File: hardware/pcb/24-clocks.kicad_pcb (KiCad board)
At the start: 2 copper layers, 89.9 x 42.4 mm, 2 parts, among them J1 Conn_01x03, J2 Conn_01x03

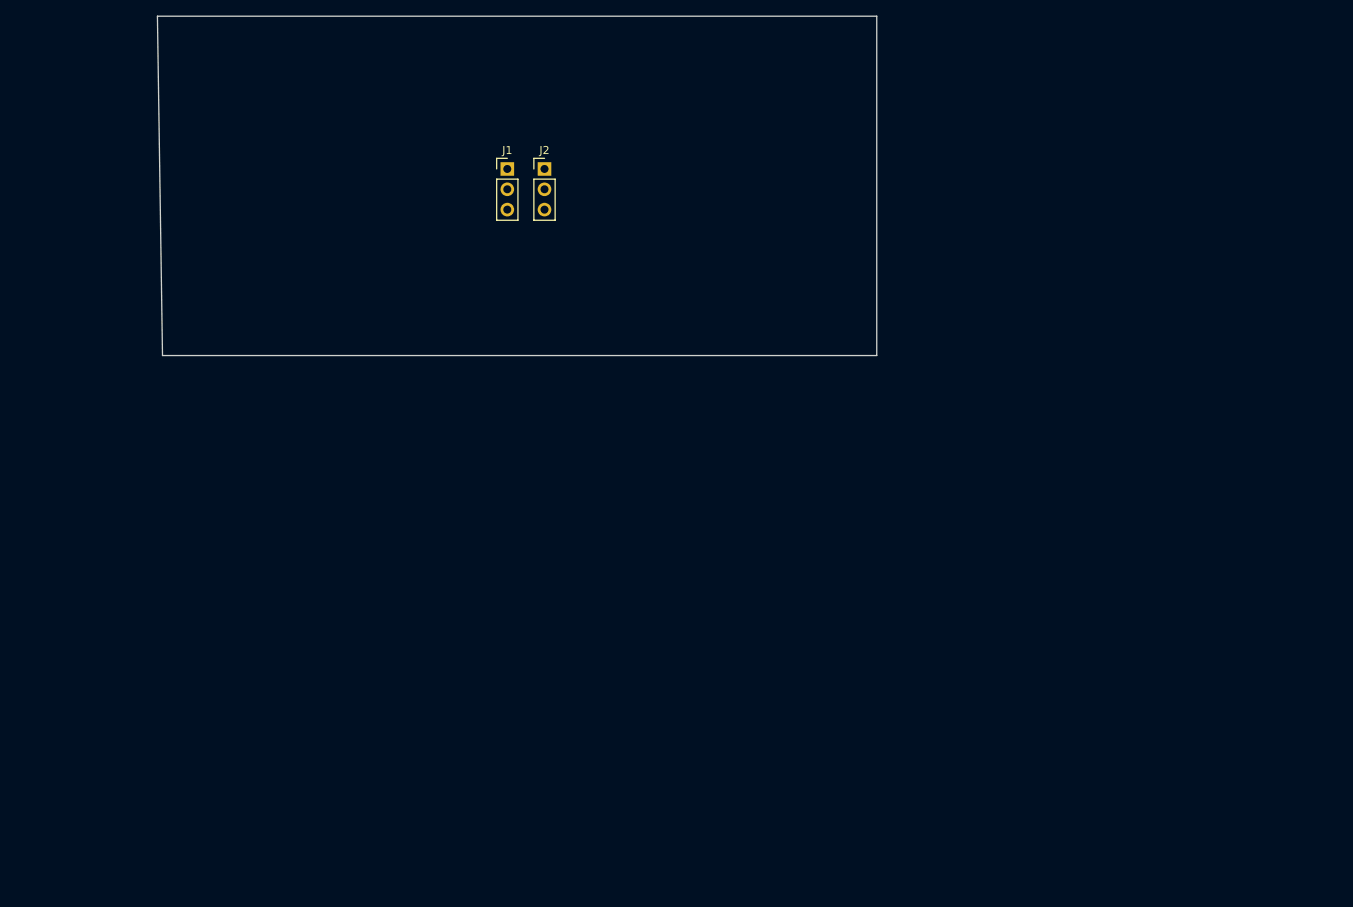
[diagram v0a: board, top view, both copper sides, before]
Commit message: Created footprints and archived project
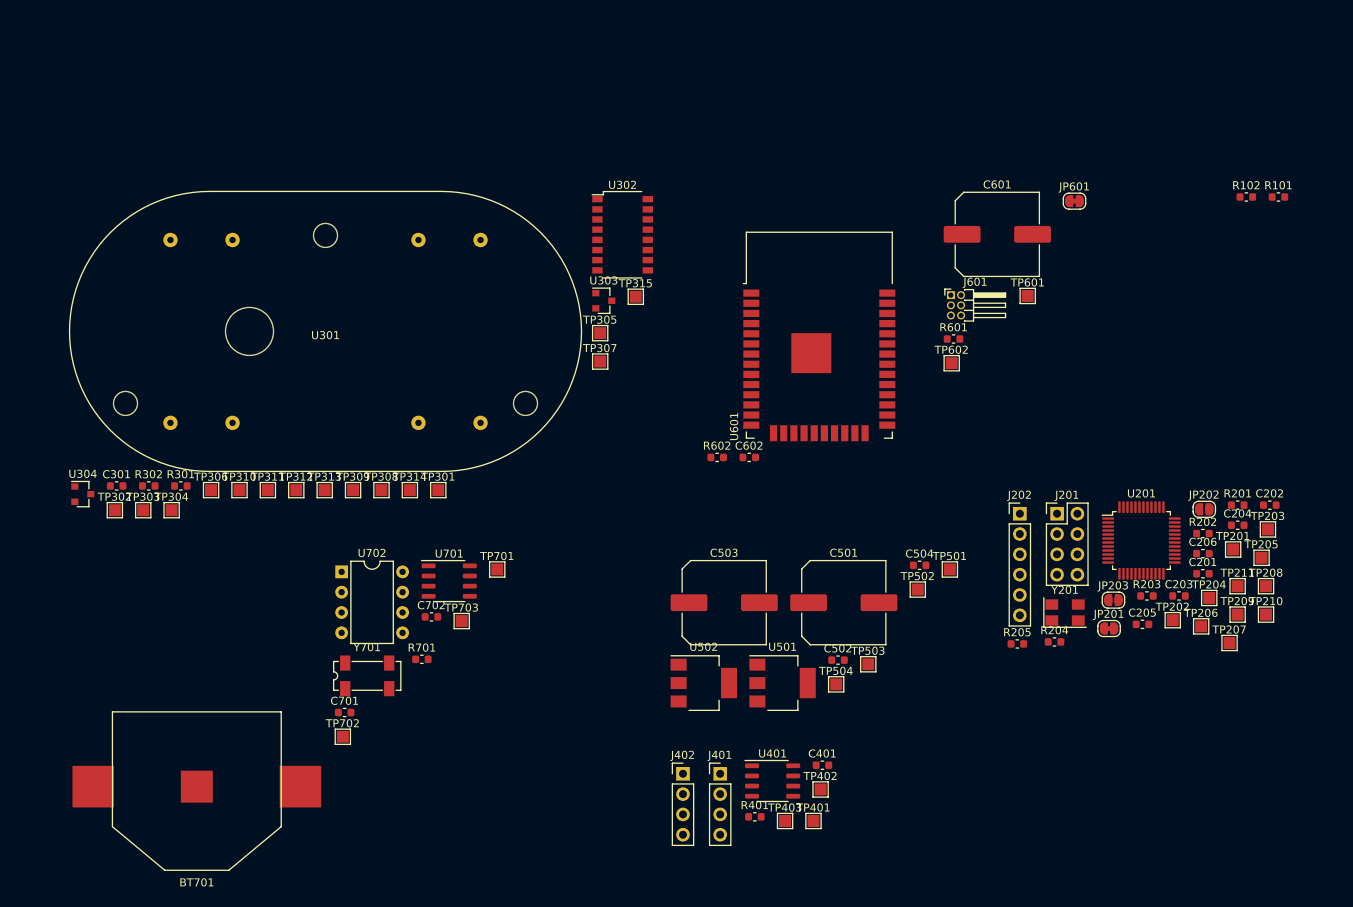
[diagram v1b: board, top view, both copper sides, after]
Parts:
- removed J1, J2: Conn_01x03, Connector_PinHeader_2.54mm:PinHeader_1x03_P2.54mm_Vertical
- added BT701: CR2032, mvl-footprints:BATT_WE_79523141, F.Cu at (106.4, 130.7)
- added C201: 100nF, Capacitor_SMD:C_0603_1608Metric, F.Cu at (232.2, 104.1)
- added C202: 100nF, Capacitor_SMD:C_0603_1608Metric, F.Cu at (240.5, 95.5)
- added C203: 100nF, Capacitor_SMD:C_0603_1608Metric, F.Cu at (229.2, 106.9)
- added C204: 100nF, Capacitor_SMD:C_0603_1608Metric, F.Cu at (236.5, 98.0)
- added C205: 20pF, Capacitor_SMD:C_0603_1608Metric, F.Cu at (224.6, 110.4)
- added C206: 20pF, Capacitor_SMD:C_0603_1608Metric, F.Cu at (232.2, 101.6)
- added C301: 100nF, Capacitor_SMD:C_0603_1608Metric, F.Cu at (96.4, 93.1)
- added C401: 100nF, Capacitor_SMD:C_0603_1608Metric, F.Cu at (184.6, 128.0)
- added C501: 22uF, Capacitor_SMD:C_Elec_10x10.2, F.Cu at (187.3, 107.7)
- added C502: 100nF, Capacitor_SMD:C_0603_1608Metric, F.Cu at (186.5, 114.9)
- added C503: 22uF, Capacitor_SMD:C_Elec_10x10.2, F.Cu at (172.3, 107.7)
- added C504: 100nF, Capacitor_SMD:C_0603_1608Metric, F.Cu at (196.7, 103.1)
- added C601: 22uF, Capacitor_SMD:C_Elec_10x10.2, F.Cu at (206.5, 61.7)
- added C602: 100nF, Capacitor_SMD:C_0603_1608Metric, F.Cu at (175.4, 89.6)
- added C701: 100nF, Capacitor_SMD:C_0603_1608Metric, F.Cu at (124.9, 121.5)
- added C702: 100nF, Capacitor_SMD:C_0603_1608Metric, F.Cu at (135.7, 109.5)
- added J201: ST-LINK, Connector_PinHeader_2.54mm:PinHeader_2x04_P2.54mm_Vertical, F.Cu at (213.9, 96.6)
- added J202: Debug UART, Connector_PinHeader_2.54mm:PinHeader_1x06_P2.54mm_Vertical, F.Cu at (209.3, 96.6)
- added J401: Conn_01x04, Connector_PinHeader_2.54mm:PinHeader_1x04_P2.54mm_Vertical, F.Cu at (171.8, 129.1)
- added J402: Conn_01x04, Connector_PinHeader_2.54mm:PinHeader_1x04_P2.54mm_Vertical, F.Cu at (167.2, 129.1)
- added J601: Conn_02x03_Odd_Even, Connector_PinHeader_1.27mm:PinHeader_2x03_P1.27mm_Horizontal, F.Cu at (200.7, 69.3)
- added JP201: Jumper_NC_Small, Jumper:SolderJumper-2_P1.3mm_Bridged_RoundedPad1.0x1.5mm, F.Cu at (220.4, 111.0)
- added JP202: Jumper_NO_Small, Jumper:SolderJumper-2_P1.3mm_Open_RoundedPad1.0x1.5mm, F.Cu at (232.3, 96.1)
- added JP203: Jumper_NO_Small, Jumper:SolderJumper-2_P1.3mm_Open_RoundedPad1.0x1.5mm, F.Cu at (221.0, 107.4)
- added JP601: Jumper_NC_Small, Jumper:SolderJumper-2_P1.3mm_Bridged_RoundedPad1.0x1.5mm, F.Cu at (216.1, 57.5)
- added R101: 5k, Resistor_SMD:R_0603_1608Metric, F.Cu at (241.6, 57.0)
- added R102: 5k, Resistor_SMD:R_0603_1608Metric, F.Cu at (237.6, 57.0)
- added R201: 4k7, Resistor_SMD:R_0603_1608Metric, F.Cu at (236.5, 95.5)
- added R202: 10k, Resistor_SMD:R_0603_1608Metric, F.Cu at (232.2, 99.1)
- added R203: 10k, Resistor_SMD:R_0603_1608Metric, F.Cu at (225.2, 106.9)
- added R204: 10k, Resistor_SMD:R_0603_1608Metric, F.Cu at (213.6, 112.6)
- added R205: 10k, Resistor_SMD:R_0603_1608Metric, F.Cu at (209.0, 112.9)
- added R301: 10k, Resistor_SMD:R_0603_1608Metric, F.Cu at (104.4, 93.1)
- added R302: 10k, Resistor_SMD:R_0603_1608Metric, F.Cu at (100.4, 93.1)
- added R401: 120E, Resistor_SMD:R_0603_1608Metric, F.Cu at (176.1, 134.5)
- added R601: 10k, Resistor_SMD:R_0603_1608Metric, F.Cu at (201.0, 74.8)
- added R602: 10k, Resistor_SMD:R_0603_1608Metric, F.Cu at (171.4, 89.6)
- added R701: 10k, Resistor_SMD:R_0603_1608Metric, F.Cu at (134.5, 114.8)
- added TP201: SWO, TestPoint:TestPoint_Pad_1.5x1.5mm, F.Cu at (235.9, 101.1)
- added TP202: uC-Rst, TestPoint:TestPoint_Pad_1.5x1.5mm, F.Cu at (228.4, 109.9)
- added TP203: SWDCLK, TestPoint:TestPoint_Pad_1.5x1.5mm, F.Cu at (240.3, 98.6)
- added TP204: SWDIO, TestPoint:TestPoint_Pad_1.5x1.5mm, F.Cu at (232.9, 107.1)
- added TP205: 3V3, TestPoint:TestPoint_Pad_1.5x1.5mm, F.Cu at (239.5, 102.1)
- added TP206: GND, TestPoint:TestPoint_Pad_1.5x1.5mm, F.Cu at (231.9, 110.7)
- added TP207: BOOT0, TestPoint:TestPoint_Pad_1.5x1.5mm, F.Cu at (235.5, 112.8)
- added TP208: BOOT1, TestPoint:TestPoint_Pad_1.5x1.5mm, F.Cu at (240.0, 105.7)
- added TP209: uC-Debug-Rx, TestPoint:TestPoint_Pad_1.5x1.5mm, F.Cu at (236.5, 109.2)
- added TP210: uC-Debug-Tx, TestPoint:TestPoint_Pad_1.5x1.5mm, F.Cu at (240.0, 109.2)
- added TP211: HW-Version, TestPoint:TestPoint_Pad_1.5x1.5mm, F.Cu at (236.5, 105.7)
- added TP301: MA1, TestPoint:TestPoint_Pad_1.5x1.5mm, F.Cu at (136.6, 93.7)
- added TP302: MA2, TestPoint:TestPoint_Pad_1.5x1.5mm, F.Cu at (96.1, 96.2)
- added TP303: M-Rst, TestPoint:TestPoint_Pad_1.5x1.5mm, F.Cu at (99.7, 96.2)
- added TP304: MA3, TestPoint:TestPoint_Pad_1.5x1.5mm, F.Cu at (103.2, 96.2)
- added TP305: M-A-CW, TestPoint:TestPoint_Pad_1.5x1.5mm, F.Cu at (156.8, 74.0)
- added TP306: M-A-Step, TestPoint:TestPoint_Pad_1.5x1.5mm, F.Cu at (108.2, 93.7)
- added TP307: MA4, TestPoint:TestPoint_Pad_1.5x1.5mm, F.Cu at (156.8, 77.6)
- added TP308: M-B-CW, TestPoint:TestPoint_Pad_1.5x1.5mm, F.Cu at (129.5, 93.7)
- added TP309: M-B-Step, TestPoint:TestPoint_Pad_1.5x1.5mm, F.Cu at (125.9, 93.7)
- added TP310: MB1, TestPoint:TestPoint_Pad_1.5x1.5mm, F.Cu at (111.7, 93.7)
- added TP311: MB2, TestPoint:TestPoint_Pad_1.5x1.5mm, F.Cu at (115.3, 93.7)
- added TP312: MB3, TestPoint:TestPoint_Pad_1.5x1.5mm, F.Cu at (118.8, 93.7)
- added TP313: MB4, TestPoint:TestPoint_Pad_1.5x1.5mm, F.Cu at (122.4, 93.7)
- added TP314: HAL-A, TestPoint:TestPoint_Pad_1.5x1.5mm, F.Cu at (133.0, 93.7)
- added TP315: HAL-B, TestPoint:TestPoint_Pad_1.5x1.5mm, F.Cu at (161.3, 69.5)
- added TP401: uC-RS485-Rx, TestPoint:TestPoint_Pad_1.5x1.5mm, F.Cu at (183.5, 135.0)
- added TP402: uC-RS485-DE, TestPoint:TestPoint_Pad_1.5x1.5mm, F.Cu at (184.4, 131.1)
- added TP403: uC-RS485-Tx, TestPoint:TestPoint_Pad_1.5x1.5mm, F.Cu at (179.9, 135.0)
- added TP501: +9V, TestPoint:TestPoint_Pad_1.5x1.5mm, F.Cu at (200.5, 103.6)
- added TP502: +5V, TestPoint:TestPoint_Pad_1.5x1.5mm, F.Cu at (196.5, 106.1)
- added TP503: +3V3, TestPoint:TestPoint_Pad_1.5x1.5mm, F.Cu at (190.3, 115.4)
- added TP504: GND, TestPoint:TestPoint_Pad_1.5x1.5mm, F.Cu at (186.3, 117.9)
- added TP601: uC-WiFi-Tx, TestPoint:TestPoint_Pad_1.5x1.5mm, F.Cu at (210.3, 69.4)
- added TP602: uC-WiFi-Rx, TestPoint:TestPoint_Pad_1.5x1.5mm, F.Cu at (200.8, 77.8)
- added TP701: I2C-SDA, TestPoint:TestPoint_Pad_1.5x1.5mm, F.Cu at (143.9, 103.6)
- added TP702: I2C-SCL, TestPoint:TestPoint_Pad_1.5x1.5mm, F.Cu at (124.6, 124.5)
- added TP703: RC2032, TestPoint:TestPoint_Pad_1.5x1.5mm, F.Cu at (139.5, 110.0)
- added U201: STM32F103C8Tx, Package_QFP:LQFP-48_7x7mm_P0.5mm, F.Cu at (224.5, 100.0)
- added U301: VID28-05, mvl-footprints:vid_28_05, F.Cu at (122.5, 73.8)
- added U302: VID66-08, Package_SO:SOP-16_4.4x10.4mm_P1.27mm, F.Cu at (159.6, 61.7)
- added U303: AH3572, Package_TO_SOT_SMD:SOT-23, F.Cu at (157.3, 70.0)
- added U304: AH3572, Package_TO_SOT_SMD:SOT-23, F.Cu at (92.1, 94.2)
- added U401: MAX3485, Package_SO:SO-8_3.9x4.9mm_P1.27mm, F.Cu at (178.4, 130.0)
- added U501: AMS1117-5.0, Package_TO_SOT_SMD:SOT-223-3_TabPin2, F.Cu at (179.6, 117.8)
- added U502: AMS1117-3.3, Package_TO_SOT_SMD:SOT-223-3_TabPin2, F.Cu at (169.8, 117.8)
- added U601: ESP32-WROOM-32D, RF_Module:ESP32-WROOM-32, F.Cu at (184.2, 77.3)
- added U701: 24LC512, Package_SO:SO-8_3.9x4.9mm_P1.27mm, F.Cu at (137.9, 105.0)
- added U702: DS1307+, Package_DIP:DIP-8_W7.62mm, F.Cu at (124.5, 103.9)
- added Y201: 8MHz, Crystal:Crystal_SMD_5032-4Pin_5.0x3.2mm, F.Cu at (214.9, 109.0)
- added Y701: 32.768kHz, Crystal:Crystal_SMD_SeikoEpson_MC306-4Pin_8.0x3.2mm, F.Cu at (127.7, 116.9)
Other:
- board outline removed

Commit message: Added motor footprint, made init pcb
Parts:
- J401, J402: footprint Connector_PinHeader_2.54mm:PinHeader_1x04_P2.54mm_Vertical -> Connector_PinHeader_2.54mm:PinHeader_1x04_P2.54mm_Horizontal
- J601: footprint Connector_PinHeader_1.27mm:PinHeader_2x03_P1.27mm_Horizontal -> Connector_PinHeader_1.27mm:PinHeader_2x03_P1.27mm_Vertical
- TP201, TP202, TP203, TP204, TP205, TP206, TP207, TP208, TP209, TP210, TP211, TP301, TP302, TP303, TP304, TP305, TP306, TP307, TP308, TP309, TP310, TP311, TP312, TP313, TP314, TP315, TP401, TP402, TP403, TP501, TP502, TP503, TP504, TP601, TP602, TP701, TP702, TP703: footprint TestPoint:TestPoint_Pad_1.5x1.5mm -> TestPoint:TestPoint_Pad_D2.0mm
- U702: footprint Package_DIP:DIP-8_W7.62mm -> Package_SO:SO-8_3.9x4.9mm_P1.27mm
- moved U301 27.3 mm to (100.6, 57.5)
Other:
- board outline added: 165.1 x 94 mm

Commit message: Finished PCB (#3)
* Created PCB outline and first placement

* Changed connectors

* Minor

* Included all 3D files

* Mixed changes

* Changed supply to 7V

* Archived PCB project

* Update 24-clocks-rescue.lib

* First placement

* Routed supplies

* Update 24-clocks.kicad_pcb

* Added routing

* Routed more nets

* Finished routing

* Archived project

* Replace hash and date

* minor

* Update pcb.yml

* Update pcb.yml

* Update pcb.yml

* Update pcb.yml

* Auto update commit date and hash

* Update output

* changed outputs

* Added layer to output

* Update hash and date also in sch

* Added caps to hall sensors

* Cleanup files
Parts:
- removed TP211: HW-Version, TestPoint:TestPoint_Pad_D2.0mm
- removed TP301: MA1, TestPoint:TestPoint_Pad_D2.0mm
- removed TP302: MA2, TestPoint:TestPoint_Pad_D2.0mm
- removed TP304: MA3, TestPoint:TestPoint_Pad_D2.0mm
- removed TP307: MA4, TestPoint:TestPoint_Pad_D2.0mm
- removed TP310: MB1, TestPoint:TestPoint_Pad_D2.0mm
- removed TP311: MB2, TestPoint:TestPoint_Pad_D2.0mm
- removed TP312: MB3, TestPoint:TestPoint_Pad_D2.0mm
- removed TP313: MB4, TestPoint:TestPoint_Pad_D2.0mm
- added C302: 100nF, Capacitor_SMD:C_0603_1608Metric, F.Cu at (130.9, 114.2)
- added C303: 100nF, Capacitor_SMD:C_0603_1608Metric, F.Cu at (124.1, 118.3)
- added C304: 100nF, Capacitor_SMD:C_0603_1608Metric, B.Cu at (152.3, 107.0)
- added C305: 100nF, Capacitor_SMD:C_0603_1608Metric, B.Cu at (152.5, 114.1)
- added D401: PESD1CAN, Package_TO_SOT_SMD:SOT-23, F.Cu at (150.4, 65.5)
- added H101: MountingHole, MountingHole:MountingHole_3.2mm_M3, F.Cu at (118.0, 74.0)
- added H102: MountingHole, MountingHole:MountingHole_3.2mm_M3, F.Cu at (172.0, 135.0)
- added H103: MountingHole, MountingHole:MountingHole_3.2mm_M3, F.Cu at (182.0, 74.0)
- added H104: MountingHole, MountingHole:MountingHole_3.2mm_M3, F.Cu at (128.0, 135.0)
- added NT701: Net-Tie_2, NetTie:NetTie-2_SMD_Pad0.5mm, F.Cu at (129.7, 101.5)
- added U305: AH3572, Package_TO_SOT_SMD:TSOT-23, B.Cu at (150.0, 107.0)
- added U306: AH3572, Package_TO_SOT_SMD:TSOT-23, B.Cu at (150.0, 114.0)
- J401, J402: value Conn_01x04 -> S4B_XH_SM4_TB; footprint Connector_PinHeader_2.54mm:PinHeader_1x04_P2.54mm_Horizontal -> mvl-footprints:JST_S4B_XH_SM4_TB
- TP201, TP202, TP203, TP204, TP205, TP206, TP207, TP208, TP209, TP210, TP303, TP305, TP306, TP308, TP309, TP314, TP315, TP401, TP402, TP403, TP501, TP502, TP503, TP504, TP601, TP602, TP701, TP702, TP703: moved to B.Cu
- U301: footprint mvl-footprints:vid_28_05 -> mvl-footprints:BK30D-R5
- U303, U304: footprint Package_TO_SOT_SMD:SOT-23 -> mvl-footprints:SOT-23-UD
- U401, U701, U702: footprint Package_SO:SO-8_3.9x4.9mm_P1.27mm -> Package_SO:SOIC-8_3.9x4.9mm_P1.27mm
- Y201: value 8MHz -> NX3225GD 8MHz; footprint Crystal:Crystal_SMD_5032-4Pin_5.0x3.2mm -> mvl-footprints:Crystal_SMD_3225-2Pin_3.2x2.5mm
- Y701: footprint Crystal:Crystal_SMD_SeikoEpson_MC306-4Pin_8.0x3.2mm -> mvl-footprints:Crystal_SMD_SeikoEpson_MC306-4Pin_8.0x3.2mm
- moved R101 129.2 mm to (130.2, 122.4), turned to 180 degrees
- moved R201 127.2 mm to (109.4, 96.2), turned to 270 degrees
- moved TP208 126.3 mm to (114.4, 92.4)
- moved C206 125.3 mm to (106.8, 102.7), turned to 90 degrees
- moved R102 124.9 mm to (130.2, 120.8), turned to 180 degrees
- moved C204 122.9 mm to (113.7, 95.6)
- moved C201 122.8 mm to (109.4, 104.6), turned to 90 degrees
- moved TP210 121.3 mm to (119.5, 122.9)
- moved TP202 120.3 mm to (109.4, 92.4)
- moved TP209 119.8 mm to (117.0, 117.8)
- moved JP202 119.7 mm to (114.4, 116.5), turned to 207 degrees
- moved TP205 119.6 mm to (122.1, 79.7)
- moved R203 118.9 mm to (106.8, 95.6), turned to 90 degrees
- moved TP203 118.6 mm to (122.1, 89.8)
- moved C205 118.3 mm to (106.8, 99.5), turned to 270 degrees
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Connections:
- net +9V renamed +7.5V
- net Net-(BT701-Pad1) renamed /RTC and Memory/Vbat
- C702 pad 2: GND -> /RTC and Memory/GND-CLK
- R701 pad 2: /RTC and Memory/RCLK -> /RTC and Memory/RTC-CLK
- U201 pad 25: (no net) -> /RTC and Memory/RTC-CLK
- U702 pad 4: GND -> /RTC and Memory/GND-CLK
- U702 pad 7: /RTC and Memory/RCLK -> /RTC and Memory/RTC-CLK
- Y201 pad 2: GND -> Net-(C206-Pad1)
- Y701 pad 2: GND -> /RTC and Memory/GND-CLK
- Y701 pad 3: GND -> /RTC and Memory/GND-CLK
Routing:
- net +3V3: track 0.00 -> 323.4 mm, vias 0 -> 23
- net +7.5V: track 0.00 -> 89.2 mm, vias 0 -> 3
- net /Mechanics/M-A-Step: track 0.00 -> 86.9 mm, vias 0 -> 4
- net /Mechanics/M-Rst: track 0.00 -> 82.5 mm, vias 0 -> 2
- net GND: track 0.00 -> 82.1 mm, vias 0 -> 134
- net /Mechanics/M-A-CW: track 0.00 -> 79.1 mm, vias 0 -> 4
- net /I2C-SDA: track 0.00 -> 78.8 mm, vias 0 -> 4
- net /I2C-SCL: track 0.00 -> 77.4 mm, vias 0 -> 4
- net /Mechanics/M-B-Step: track 0.00 -> 64.9 mm, vias 0 -> 5
- net /Mechanics/MB3: track 0.00 -> 64.6 mm, vias 0 -> 1
- net /RTC and Memory/Vbat: track 0.00 -> 62.6 mm, vias 0 -> 1
- net /Mechanics/M-B-CW: track 0.00 -> 60.7 mm, vias 0 -> 3
- net /Com Bus/uC-RS485-DE: track 0.00 -> 57.5 mm, vias 0 -> 2
- net /Com Bus/uC-RS485-Tx: track 0.00 -> 55.7 mm, vias 0 -> 2
- net /Mechanics/HAL-B: track 0.00 -> 55.2 mm, vias 0 -> 1
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- added copper zone on B.Cu, net +3V3
- added copper zone on F.Cu, net +3V3
- added copper zone on B.Cu, net +5V
- added copper zone on F.Cu, net +5V
- added copper zone on F.Cu, net /RTC and Memory/GND-CLK
- added copper zone on B.Cu, net /RTC and Memory/RTC-CLK
- added copper zone on B.Cu, net GND
- added copper zone on F.Cu, net GND
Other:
- board size 165.1 x 94 mm -> 94 x 84 mm
- net class Default: clearance 0.2 -> 0.15; trace_width 0.25 -> 0.2
- net class Motor added: clearance 0.2, trace_width 0.3, via_dia 0.8, via_drill 0.4
- net class Power added: clearance 0.2, trace_width 0.5, via_dia 1, via_drill 0.5
- net class RS485 added: clearance 0.2, trace_width 0.3, via_dia 0.8, via_drill 0.4
- rule pad_to_mask_clearance: 0.051 -> 0
- rule trace_clearance: 0.2 -> 0.15
- board text added: "24 Clocks"
- board text added: "GITDATE"
- board text added: "GITHASH"
- board text added: "JLCJLCJLCJLC"
- board text added: "Martin vL"

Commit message: Steppers running + pass through master
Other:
- net class Default removed
- net class Motor removed
- net class Power removed
- net class RS485 removed
